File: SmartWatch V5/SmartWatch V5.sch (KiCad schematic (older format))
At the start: 57 parts, among them J1 10118192-0001LF, J10 TestPad, J2 , J7 TestPad, J8 TestPad, J9 TestPad, Q1 FDN340P, Q2 MMBT3904, Q3 MMBT3904, Q4 2N7002K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

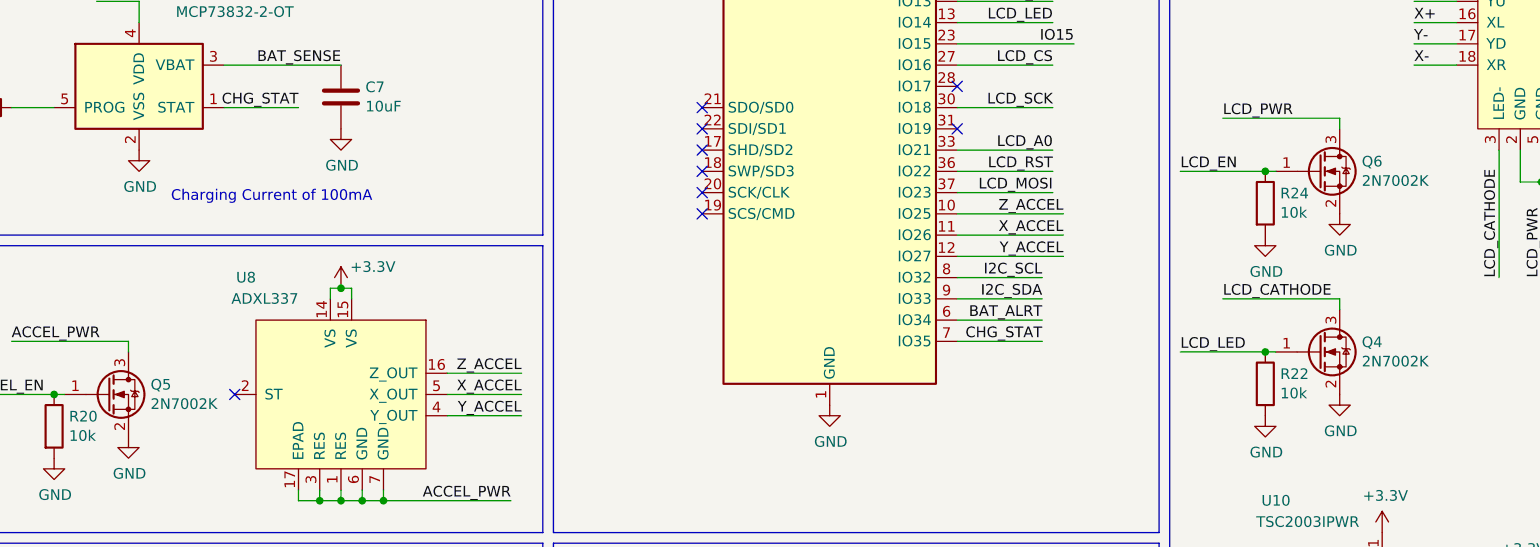
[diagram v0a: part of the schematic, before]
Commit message: Added datasheet for 2n7002K
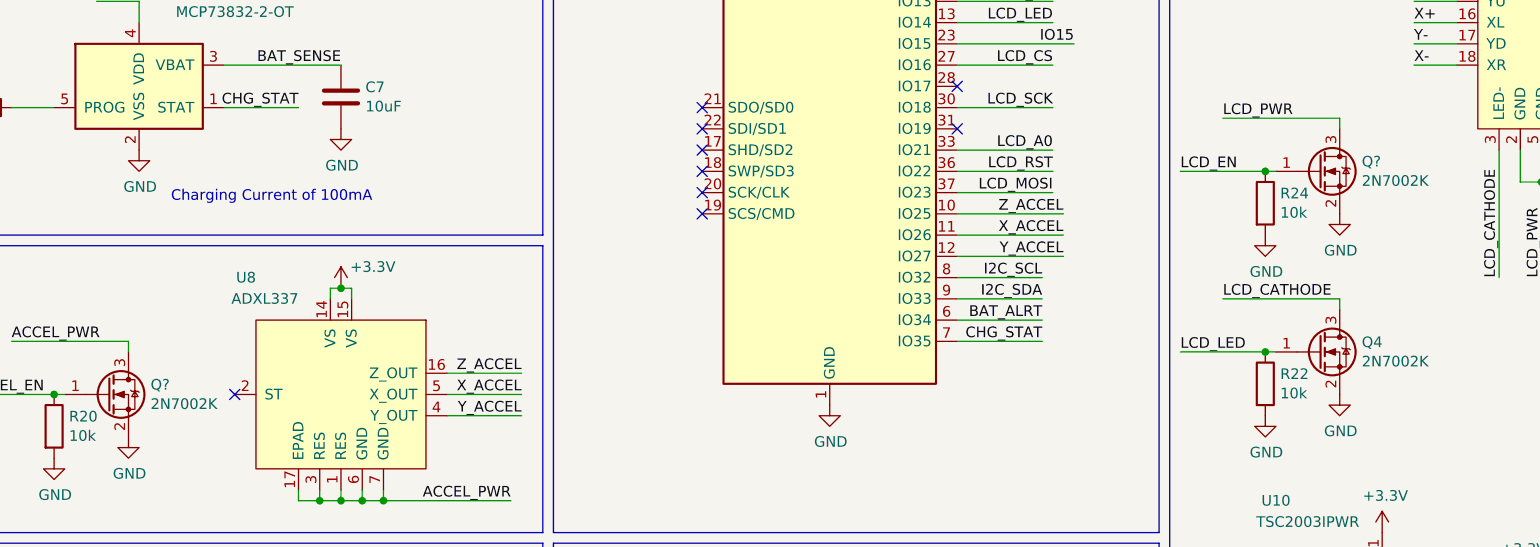
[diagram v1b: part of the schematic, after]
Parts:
- removed Q5, Q6: 2N7002K, Package_TO_SOT_SMD:SOT-23, symbol Device:Q_NMOS_GSD
- added Q? (x2): 2N7002K, Package_TO_SOT_SMD:SOT-23, symbol Device:Q_NMOS_GSD
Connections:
- net ACCEL_EN: now also Q?.1 (G)
- net ACCEL_PWR: now also Q?.3 (D)
- net GND: now also Q?.2 (S), Q?.2 (S)
- net LCD_EN: now also Q?.1 (G)
- net LCD_PWR: now also Q?.3 (D)
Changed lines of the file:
@@
 F 1 "2N7002K" H 9854 3755 50  0000 L CNN
 F 2 "Package_TO_SOT_SMD:SOT-23" H 9850 3900 50  0001 C CNN
-F 3 "~" H 9650 3800 50  0001 C CNN
+F 3 "https://www.onsemi.com/pub/Collateral/2N7002K-D.pdf" H 9650 3800 50  0001 C CNN
 F 4 "2N7002KCT-ND" H 9650 3800 50  0001 C CNN "digikey"
 	1    9650 3800
@@
 $EndComp
 $Comp
-L Device:Q_NMOS_GSD Q6
-U 1 1 5F4B0D43
-P 9650 2950
-F 0 "Q6" H 9854 2996 50  0000 L CNN
-F 1 "2N7002K" H 9854 2905 50  0000 L CNN
-F 2 "Package_TO_SOT_SMD:SOT-23" H 9850 3050 50  0001 C CNN
-F 3 "~" H 9650 2950 50  0001 C CNN
-F 4 "2N7002KCT-ND" H 9650 2950 50  0001 C CNN "digikey"
-	1    9650 2950
-	1    0    0    -1
-$EndComp
-$Comp
 L power:GND #PWR07
 U 1 1 5F4B0D49
@@
 Text Label 3300 4000 0    50   ~ 0
 ACCEL_EN
-$Comp
-L Device:Q_NMOS_GSD Q5
-U 1 1 5F503F1E
-P 3950 4000
-F 0 "Q5" H 4154 4046 50  0000 L CNN
-F 1 "2N7002K" H 4154 3955 50  0000 L CNN
-F 2 "Package_TO_SOT_SMD:SOT-23" H 4150 4100 50  0001 C CNN
-F 3 "~" H 3950 4000 50  0001 C CNN
-F 4 "2N7002KCT-ND" H 3950 4000 50  0001 C CNN "digikey"
-	1    3950 4000
-	1    0    0    -1
-$EndComp
 $Comp
 L power:GND #PWR05
@@
 Wire Bus Line
 	3200 3300 6000 3300
+$Comp
+L Device:Q_NMOS_GSD Q?
+U 1 1 5F899AC5
+P 9650 2950
+F 0 "Q?" H 9854 2996 50  0000 L CNN
+F 1 "2N7002K" H 9854 2905 50  0000 L CNN
+F 2 "Package_TO_SOT_SMD:SOT-23" H 9850 3050 50  0001 C CNN
+F 3 "https://www.onsemi.com/pub/Collateral/2N7002K-D.pdf" H 9650 2950 50  0001 C CNN
+F 4 "2N7002KCT-ND" H 9650 2950 50  0001 C CNN "digikey"
+	1    9650 2950
+	1    0    0    -1
+$EndComp
+$Comp
+L Device:Q_NMOS_GSD Q?
+U 1 1 5F899FA0
+P 3950 4000
+F 0 "Q?" H 4154 4046 50  0000 L CNN
+F 1 "2N7002K" H 4154 3955 50  0000 L CNN
+F 2 "Package_TO_SOT_SMD:SOT-23" H 4150 4100 50  0001 C CNN
+F 3 "https://www.onsemi.com/pub/Collateral/2N7002K-D.pdf" H 3950 4000 50  0001 C CNN
+F 4 "2N7002KCT-ND" H 3950 4000 50  0001 C CNN "digikey"
+	1    3950 4000
+	1    0    0    -1
+$EndComp
 $EndSCHEMATC

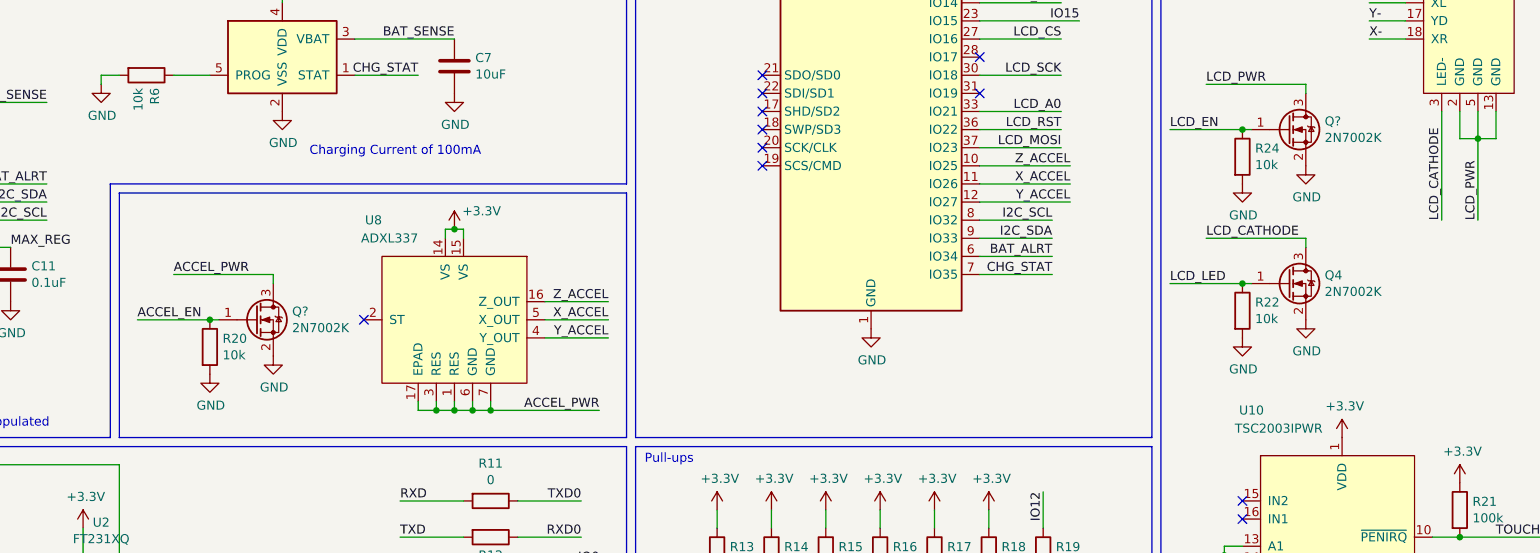
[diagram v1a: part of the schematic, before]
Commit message: Switched 2N7002K with FDN028N20 which has a significantly lower RDSon
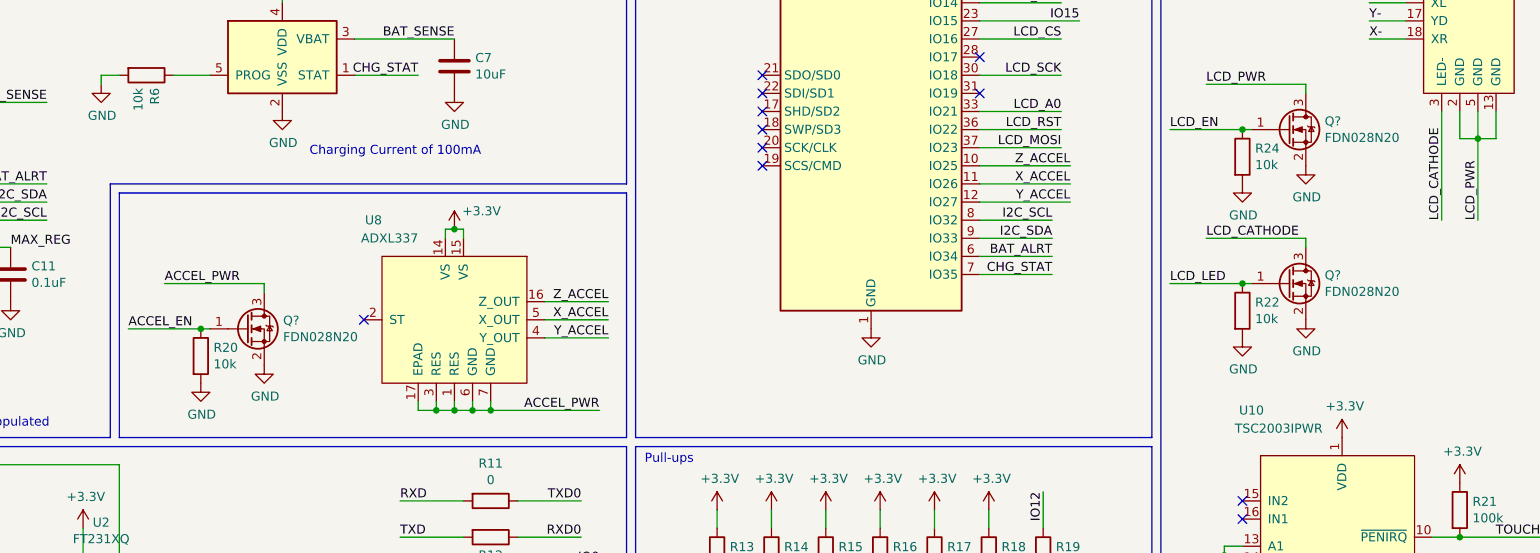
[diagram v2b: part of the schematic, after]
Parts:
- removed Q4, Q? (x2): 2N7002K, Package_TO_SOT_SMD:SOT-23, symbol Device:Q_NMOS_GSD
- added Q? (x3): FDN028N20, Package_TO_SOT_SMD:SOT-23, symbol Device:Q_NMOS_GSD
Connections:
- net ACCEL_EN: now also Q?.1 (G)
- net ACCEL_PWR: now also Q?.3 (D)
- net GND: now also Q?.2 (S), Q?.2 (S), Q?.2 (S)
- net LCD_CATHODE: now also Q?.3 (D)
- net LCD_EN: now also Q?.1 (G)
- net LCD_LED: now also Q?.1 (G)
- net LCD_PWR: now also Q?.3 (D)
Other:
- moved on the sheet: R20
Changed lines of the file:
@@
 LCD_LED
-$Comp
-L Device:Q_NMOS_GSD Q4
-U 1 1 5EFC26EF
-P 9650 3800
-F 0 "Q4" H 9854 3846 50  0000 L CNN
-F 1 "2N7002K" H 9854 3755 50  0000 L CNN
-F 2 "Package_TO_SOT_SMD:SOT-23" H 9850 3900 50  0001 C CNN
-F 3 "https://www.onsemi.com/pub/Collateral/2N7002K-D.pdf" H 9650 3800 50  0001 C CNN
-F 4 "2N7002KCT-ND" H 9650 3800 50  0001 C CNN "digikey"
-	1    9650 3800
-	1    0    0    -1
-$EndComp
 $Comp
 L power:GND #PWR0123
@@
 L Device:R R20
 U 1 1 5F503F15
-P 3700 4150
-F 0 "R20" H 3770 4196 50  0000 L CNN
-F 1 "10k" H 3770 4105 50  0000 L CNN
-F 2 "Resistor_SMD:R_0603_1608Metric" V 3630 4150 50  0001 C CNN
-F 3 "~" H 3700 4150 50  0001 C CNN
-F 4 "311-10.0KCRCT-ND" H 3700 4150 50  0001 C CNN "digikey"
-	1    3700 4150
-	1    0    0    -1
-$EndComp
-Text Label 3500 3750 0    50   ~ 0
+P 3650 4200
+F 0 "R20" H 3720 4246 50  0000 L CNN
+F 1 "10k" H 3720 4155 50  0000 L CNN
+F 2 "Resistor_SMD:R_0603_1608Metric" V 3580 4200 50  0001 C CNN
+F 3 "~" H 3650 4200 50  0001 C CNN
+F 4 "311-10.0KCRCT-ND" H 3650 4200 50  0001 C CNN "digikey"
+	1    3650 4200
+	1    0    0    -1
+$EndComp
+Text Label 3450 3800 0    50   ~ 0
 ACCEL_PWR
-Text Label 3300 4000 0    50   ~ 0
+Text Label 3250 4050 0    50   ~ 0
 ACCEL_EN
 $Comp
 L power:GND #PWR05
 U 1 1 5F503F24
-P 4050 4200
-F 0 "#PWR05" H 4050 3950 50  0001 C CNN
-F 1 "GND" H 4055 4027 50  0000 C CNN
-F 2 "" H 4050 4200 50  0001 C CNN
-F 3 "" H 4050 4200 50  0001 C CNN
-	1    4050 4200
+P 4000 4250
+F 0 "#PWR05" H 4000 4000 50  0001 C CNN
+F 1 "GND" H 4005 4077 50  0000 C CNN
+F 2 "" H 4000 4250 50  0001 C CNN
+F 3 "" H 4000 4250 50  0001 C CNN
+	1    4000 4250
 	1    0    0    -1
 $EndComp
@@
 L power:GND #PWR04
 U 1 1 5F503F2A
-P 3700 4300
-F 0 "#PWR04" H 3700 4050 50  0001 C CNN
-F 1 "GND" H 3705 4127 50  0000 C CNN
-F 2 "" H 3700 4300 50  0001 C CNN
-F 3 "" H 3700 4300 50  0001 C CNN
-	1    3700 4300
-	1    0    0    -1
-$EndComp
-Connection ~ 3700 4000
-Wire Wire Line
-	3700 4000 3750 4000
-Wire Wire Line
-	3300 4000 3700 4000
-Wire Wire Line
-	4050 3800 4050 3750
-Wire Wire Line
-	3500 3750 4050 3750
+P 3650 4350
+F 0 "#PWR04" H 3650 4100 50  0001 C CNN
+F 1 "GND" H 3655 4177 50  0000 C CNN
+F 2 "" H 3650 4350 50  0001 C CNN
+F 3 "" H 3650 4350 50  0001 C CNN
+	1    3650 4350
+	1    0    0    -1
+$EndComp
+Connection ~ 3650 4050
+Wire Wire Line
+	3650 4050 3700 4050
+Wire Wire Line
+	3250 4050 3650 4050
+Wire Wire Line
+	4000 3850 4000 3800
+Wire Wire Line
+	3450 3800 4000 3800
 Wire Wire Line
 	5250 4500 5850 4500
@@
 $Comp
 L Device:Q_NMOS_GSD Q?
-U 1 1 5F899AC5
+U 1 1 5F89B605
+P 9650 3800
+F 0 "Q?" H 9854 3846 50  0000 L CNN
+F 1 "FDN028N20" H 9854 3755 50  0000 L CNN
+F 2 "Package_TO_SOT_SMD:SOT-23" H 9850 3900 50  0001 C CNN
+F 3 "https://www.onsemi.com/pub/Collateral/FDN028N20-D.pdf" H 9650 3800 50  0001 C CNN
+F 4 "FDN028N20OSCT-ND" H 9650 3800 50  0001 C CNN "digikey"
+	1    9650 3800
+	1    0    0    -1
+$EndComp
+$Comp
+L Device:Q_NMOS_GSD Q?
+U 1 1 5F89CF73
 P 9650 2950
 F 0 "Q?" H 9854 2996 50  0000 L CNN
-F 1 "2N7002K" H 9854 2905 50  0000 L CNN
+F 1 "FDN028N20" H 9854 2905 50  0000 L CNN
 F 2 "Package_TO_SOT_SMD:SOT-23" H 9850 3050 50  0001 C CNN
-F 3 "https://www.onsemi.com/pub/Collateral/2N7002K-D.pdf" H 9650 2950 50  0001 C CNN
-F 4 "2N7002KCT-ND" H 9650 2950 50  0001 C CNN "digikey"
+F 3 "https://www.onsemi.com/pub/Collateral/FDN028N20-D.pdf" H 9650 2950 50  0001 C CNN
+F 4 "FDN028N20OSCT-ND" H 9650 2950 50  0001 C CNN "digikey"
 	1    9650 2950
 	1    0    0    -1
@@
 $Comp
 L Device:Q_NMOS_GSD Q?
-U 1 1 5F899FA0
-P 3950 4000
-F 0 "Q?" H 4154 4046 50  0000 L CNN
-F 1 "2N7002K" H 4154 3955 50  0000 L CNN
-F 2 "Package_TO_SOT_SMD:SOT-23" H 4150 4100 50  0001 C CNN
-F 3 "https://www.onsemi.com/pub/Collateral/2N7002K-D.pdf" H 3950 4000 50  0001 C CNN
-F 4 "2N7002KCT-ND" H 3950 4000 50  0001 C CNN "digikey"
-	1    3950 4000
-	1    0    0    -1
-$EndComp
+U 1 1 5F89D454
+P 3900 4050
+F 0 "Q?" H 4104 4096 50  0000 L CNN
+F 1 "FDN028N20" H 4104 4005 50  0000 L CNN
+F 2 "Package_TO_SOT_SMD:SOT-23" H 4100 4150 50  0001 C CNN
+F 3 "https://www.onsemi.com/pub/Collateral/FDN028N20-D.pdf" H 3900 4050 50  0001 C CNN
+F 4 "FDN028N20OSCT-ND" H 3900 4050 50  0001 C CNN "digikey"
+	1    3900 4050
+	1    0    0    -1
+$EndComp

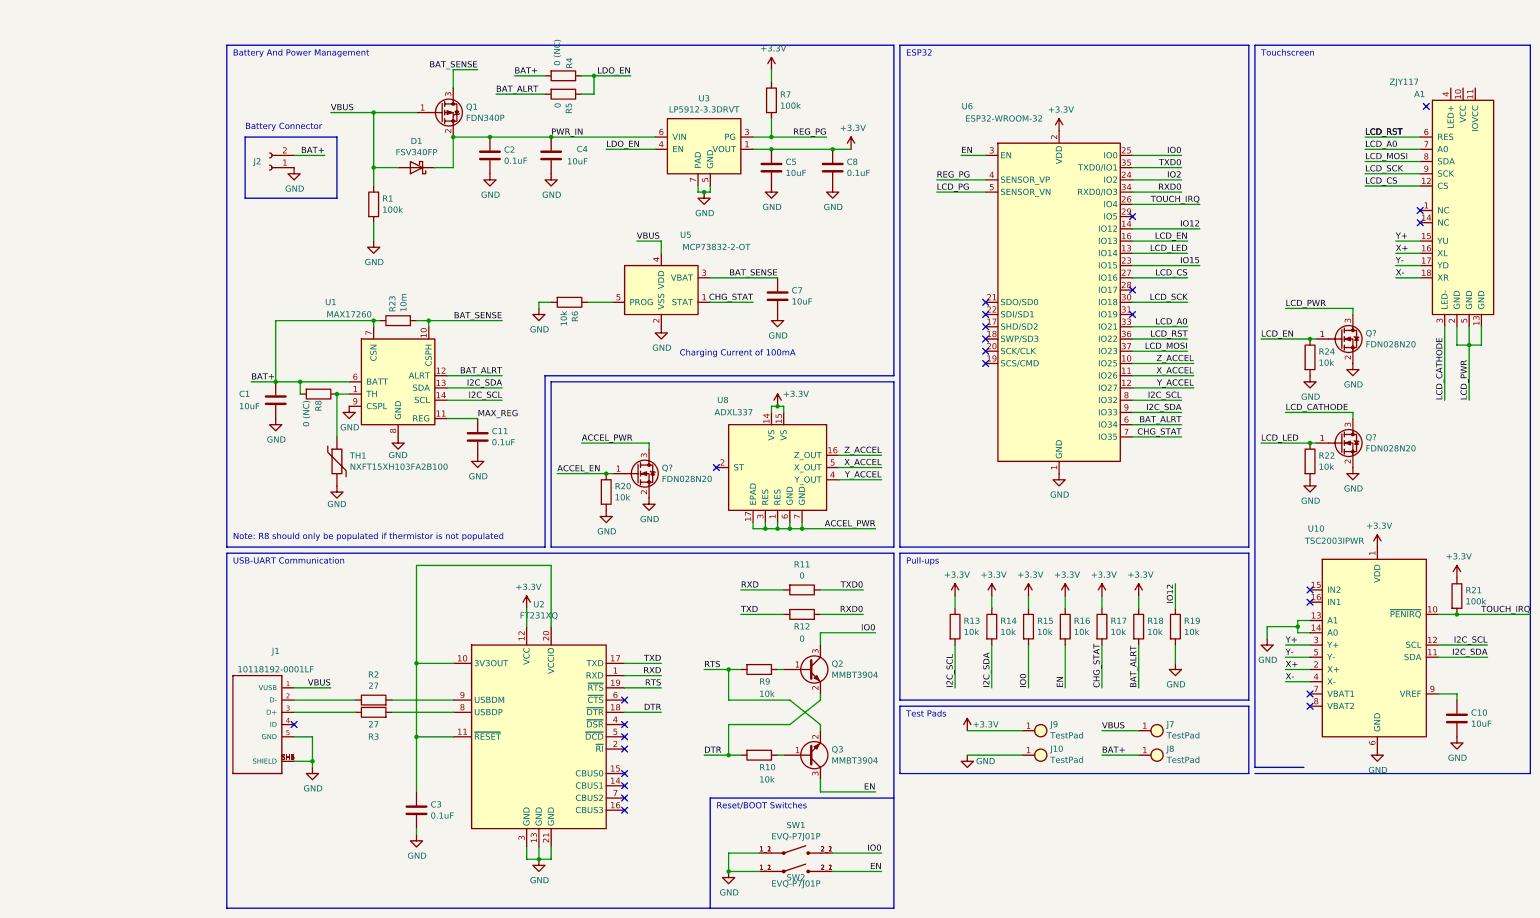
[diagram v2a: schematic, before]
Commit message: Added Surge/ESD protection to USB port
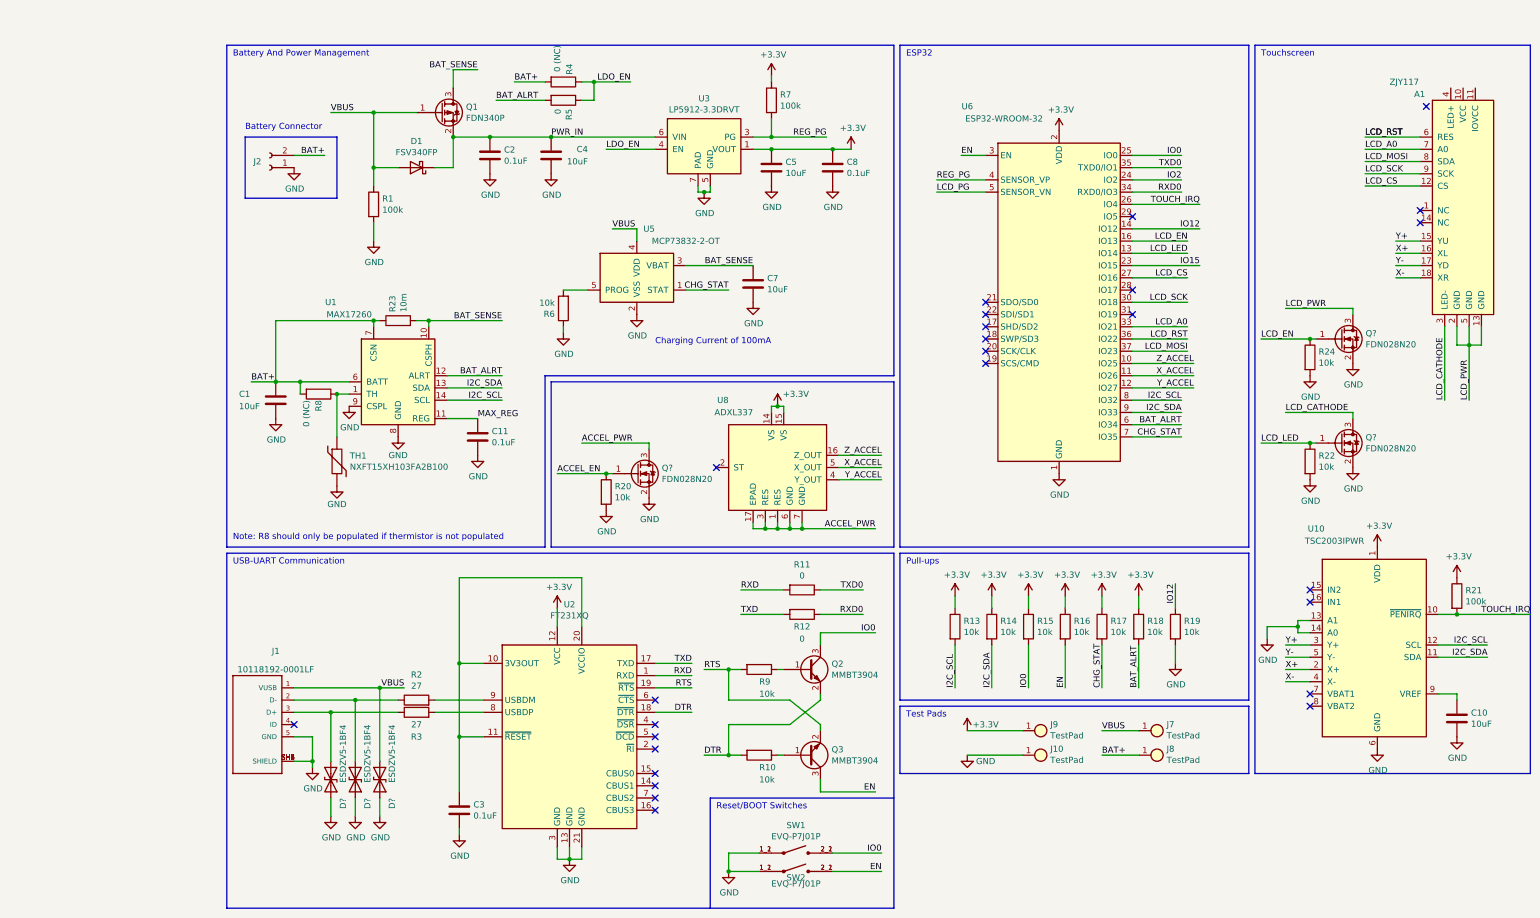
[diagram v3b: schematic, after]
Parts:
- added D? (x3): ESDZV5-1BF4, Diode_SMD:D_0201_0603Metric, symbol Device:D_TVS
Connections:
- net GND: now also R6.1, D?.2 (A2), D?.2 (A2), D?.2 (A2); no longer R6.2
- net VBUS: now also D?.1 (A1)
- net at J1.2 (D-), R2.1: now also D?.1 (A1)
- net at J1.3 (D+), R3.1: now also D?.1 (A1)
- net at U5.5 (PROG): now also R6.2; no longer R6.1
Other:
- moved on the sheet: C3, C7, R2, R3, R4, R5, R6, U2, U5
